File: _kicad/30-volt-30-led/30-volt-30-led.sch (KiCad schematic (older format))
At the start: 26 parts, among them Q1 2N2905, U1 LM3914V, U2 LM3914V, U3 LM3914V

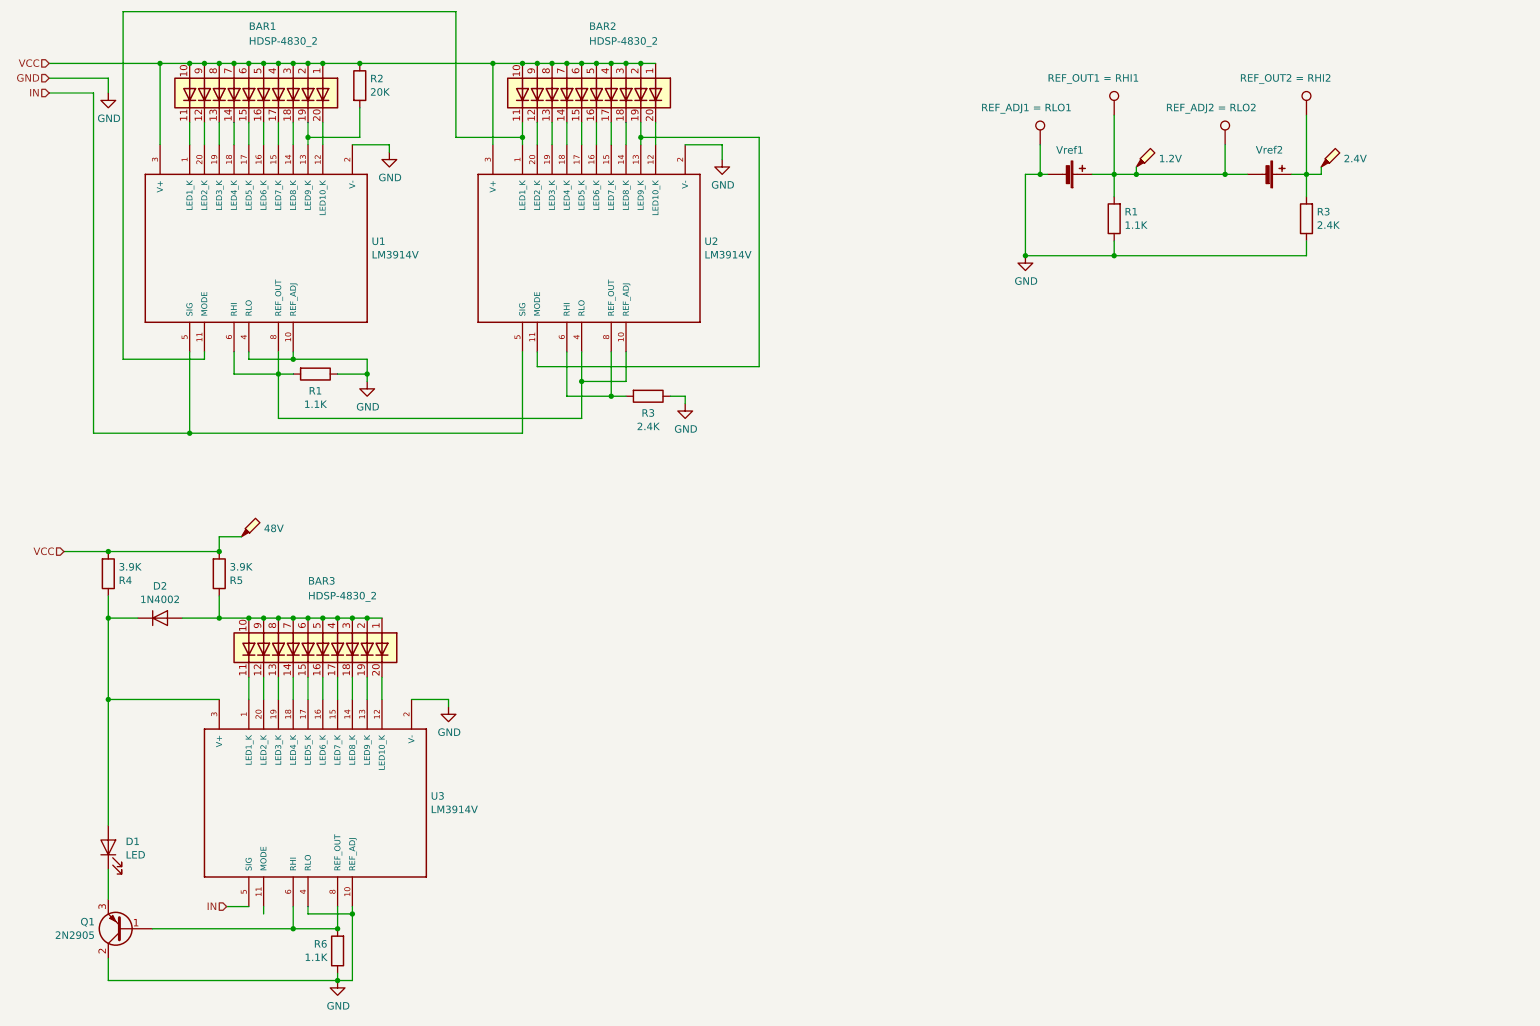
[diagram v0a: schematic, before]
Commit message: Almost done with the 30 volt 30 LED post
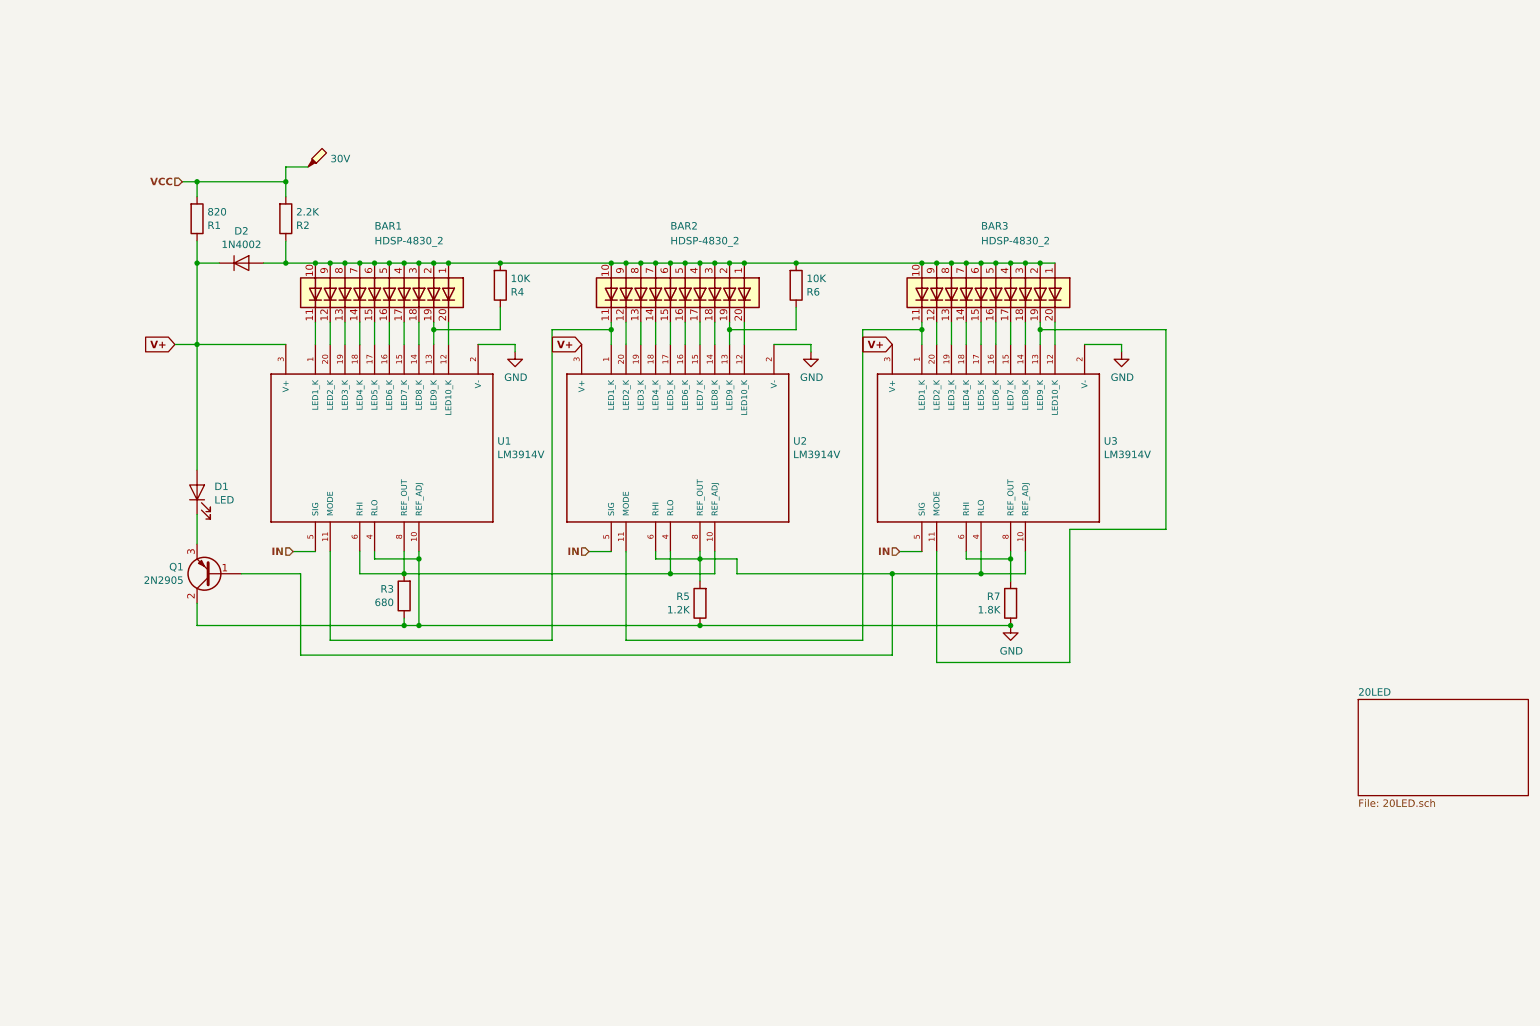
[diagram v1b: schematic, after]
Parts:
- removed BAR1: HDSP-4830_2, Display:HDSP-4830, symbol LED:HDSP-4830_2
- removed BT1: Vref1, symbol Device:Battery_Cell
- removed BT2: Vref2, symbol Device:Battery_Cell
- removed R1 (x2): 1.1K, symbol 30-volt-30-led-rescue:R-CapacitorTester-rescue
- removed R2: 20K, symbol 30-volt-30-led-rescue:R-CapacitorTester-rescue
- removed R3 (x2): 2.4K, symbol 30-volt-30-led-rescue:R-CapacitorTester-rescue
- removed TP2: REF_ADJ1 = RLO1, symbol Connector:TestPoint
- removed TP3: REF_OUT1 = RHI1, symbol Connector:TestPoint
- removed TP4: 1.2V, symbol Connector:TestPoint_Probe
- removed TP5: REF_ADJ2 = RLO2, symbol Connector:TestPoint
- removed TP6: REF_OUT2 = RHI2, symbol Connector:TestPoint
- removed TP7: 2.4V, symbol Connector:TestPoint_Probe
- removed U1: LM3914V, PLCC127P990X990X457-20N, symbol LM3914V:LM3914V
- added BAR3: HDSP-4830_2, Display:HDSP-4830, symbol LED:HDSP-4830_2
- added R4, R6: 10K, symbol 30-volt-30-led-rescue:R-CapacitorTester-rescue
- added R5: 1.2K, symbol 30-volt-30-led-rescue:R-CapacitorTester-rescue
- added R7: 1.8K, symbol 30-volt-30-led-rescue:R-CapacitorTester-rescue
- added U3: LM3914V, PLCC127P990X990X457-20N, symbol LM3914V:LM3914V
- R1: renamed from R4; value 3.9K -> 820
- R2: renamed from R5; value 3.9K -> 2.2K
- R3: renamed from R6; value 1.1K -> 680
- TP1: value 48V -> 30V
- renumbered BAR3 to BAR1, U3 to U1
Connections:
- net GND: now also R5.1, R7.1, U3.2 (V-)
- net IN: now also U3.5 (SIG)
- net VCC: no longer BAR2.1 (A), BAR2.10 (A), BAR2.2 (A), BAR2.3 (A), BAR2.4 (A), BAR2.5 (A), BAR2.6 (A), BAR2.7 (A), BAR2.8 (A), BAR2.9 (A), U2.3 (V+)
- net at BAR2.11 (K), U2.1 (LED1_K): now also U1.11 (MODE)
- net at BAR2.19 (K), U2.13 (LED9_K): now also R6.1; no longer U2.11 (MODE)
- net at U2.10 (REF_ADJ), U2.4 (RLO): now also R3.2, U1.6 (RHI), U1.8 (REF_OUT)
- net at U2.6 (RHI), U2.8 (REF_OUT): now also Q1.1 (B), R5.2, U3.10 (REF_ADJ), U3.4 (RLO)
- net at BAR1.1 (A), BAR1.10 (A), BAR1.2 (A)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: now also BAR2.1 (A), BAR2.10 (A), BAR2.2 (A), BAR2.3 (A), BAR2.4 (A), BAR2.5 (A), BAR2.6 (A), BAR2.7 (A), BAR2.8 (A), BAR2.9 (A), BAR3.1 (A), BAR3.10 (A), BAR3.2 (A), BAR3.3 (A), BAR3.4 (A), BAR3.5 (A), BAR3.6 (A), BAR3.7 (A), BAR3.8 (A), BAR3.9 (A), R4.2, R6.2
- net at BAR1.19 (K), U1.13 (LED9_K): now also R4.1
- net V+: now reaches D1.2 (A), D2.1 (K), R1.1, U1.3 (V+)
- net V+: now also U2.3 (V+), U3.3 (V+)
- new net: BAR3.11 (K), U2.11 (MODE), U3.1 (LED1_K)
- new net: BAR3.12 (K), U3.20 (LED2_K)
- new net: BAR3.13 (K), U3.19 (LED3_K)
- new net: BAR3.14 (K), U3.18 (LED4_K)
- new net: BAR3.15 (K), U3.17 (LED5_K)
- new net: BAR3.16 (K), U3.16 (LED6_K)
- new net: BAR3.17 (K), U3.15 (LED7_K)
- new net: BAR3.18 (K), U3.14 (LED8_K)
- new net: BAR3.19 (K), U3.11 (MODE), U3.13 (LED9_K)
- new net: BAR3.20 (K), U3.12 (LED10_K)
- new net: R7.2, U3.6 (RHI), U3.8 (REF_OUT)
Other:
- moved on the sheet: BAR1, D1, D2, Q1, R1, R2, R3, U1
